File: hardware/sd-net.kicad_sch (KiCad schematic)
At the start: 13 parts, among them U1 GL823K-HCY04

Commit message: stop downward net labels colliding with their own symbols
Global labels below a pin were justified so they rendered back up over the part
they belong to: R1's LED_A sat on the resistor body and PWR_FLAG's GND was
inside the flag graphic. Flipped the justification on downward labels, then
moved R1, LED1 and the flag into their own row -- R1 had been directly below
C1, so once the labels pointed the right way C1's GND ran into R1's VDD.

Verified by rendering the PDF and inspecting it rather than by eye. ERC clean,
netlist unchanged and still passing.
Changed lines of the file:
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@@
 		(instances
 			(project "sd-net"
-				(path "/1ebe58e1-8cab-4a64-8f47-26625183a810"
+				(path "/c22e1f68-a25e-4be5-9891-1892730bf935"
 					(reference "U1") (unit 1)
 				)
@@
 		(instances
 			(project "sd-net"
-				(path "/1ebe58e1-8cab-4a64-8f47-26625183a810"
+				(path "/c22e1f68-a25e-4be5-9891-1892730bf935"
 					(reference "CARD1") (unit 1)
 				)
@@
 		(instances
 			(project "sd-net"
-				(path "/1ebe58e1-8cab-4a64-8f47-26625183a810"
+				(path "/c22e1f68-a25e-4be5-9891-1892730bf935"
 					(reference "USB1") (unit 1)
 				)
@@
 		(instances
 			(project "sd-net"
-				(path "/1ebe58e1-8cab-4a64-8f47-26625183a810"
+				(path "/c22e1f68-a25e-4be5-9891-1892730bf935"
 					(reference "C1") (unit 1)
 				)
@@
 		(instances
 			(project "sd-net"
-				(path "/1ebe58e1-8cab-4a64-8f47-26625183a810"
+				(path "/c22e1f68-a25e-4be5-9891-1892730bf935"
 					(reference "C4") (unit 1)
 				)
@@
 		(instances
 			(project "sd-net"
-				(path "/1ebe58e1-8cab-4a64-8f47-26625183a810"
+				(path "/c22e1f68-a25e-4be5-9891-1892730bf935"
 					(reference "C2") (unit 1)
 				)
@@
 		(instances
 			(project "sd-net"
-				(path "/1ebe58e1-8cab-4a64-8f47-26625183a810"
+				(path "/c22e1f68-a25e-4be5-9891-1892730bf935"
 					(reference "C5") (unit 1)
 				)
@@
 		(instances
 			(project "sd-net"
-				(path "/1ebe58e1-8cab-4a64-8f47-26625183a810"
+				(path "/c22e1f68-a25e-4be5-9891-1892730bf935"
 					(reference "C6") (unit 1)
 				)
@@
 		(instances
 			(project "sd-net"
-				(path "/1ebe58e1-8cab-4a64-8f47-26625183a810"
+				(path "/c22e1f68-a25e-4be5-9891-1892730bf935"
 					(reference "C8") (unit 1)
 				)
@@
 		(instances
 			(project "sd-net"
-				(path "/1ebe58e1-8cab-4a64-8f47-26625183a810"
+				(path "/c22e1f68-a25e-4be5-9891-1892730bf935"
 					(reference "C3") (unit 1)
 				)
@@
 		(instances
 			(project "sd-net"
-				(path "/1ebe58e1-8cab-4a64-8f47-26625183a810"
+				(path "/c22e1f68-a25e-4be5-9891-1892730bf935"
 					(reference "C7") (unit 1)
 				)
@@
 	(symbol
 		(lib_id "Device:R")
-		(at 68.58 173.99 0)
+		(at 68.58 184.15 0)
 		(unit 1)
 		(exclude_from_sim no)
@@
 		(fields_autoplaced yes)
 		(property "Reference" "R1"
-			(at 72.39 172.72 0)
+			(at 72.39 182.88 0)
 			(effects (font (size 1.27 1.27)) (justify left))
 		)
 		(property "Value" "220"
-			(at 72.39 175.26 0)
+			(at 72.39 185.42 0)
 			(effects (font (size 1.27 1.27)) (justify left))
 		)
 		(property "Footprint" "Resistor_SMD:R_0603_1608Metric"
-			(at 68.58 173.99 0)
+			(at 68.58 184.15 0)
 			(effects (font (size 1.27 1.27)) (hide yes))
 		)
 		(property "LCSC" "C22962"
-			(at 68.58 173.99 0)
-			(effects (font (size 1.27 1.27)) (hide yes))
-		)
-		(instances
-			(project "sd-net"
-				(path "/1ebe58e1-8cab-4a64-8f47-26625183a810"
+			(at 68.58 184.15 0)
+			(effects (font (size 1.27 1.27)) (hide yes))
+		)
+		(instances
+			(project "sd-net"
+				(path "/c22e1f68-a25e-4be5-9891-1892730bf935"
 					(reference "R1") (unit 1)
 				)
@@
 	(symbol
 		(lib_id "Device:LED")
-		(at 96.52 173.99 0)
+		(at 109.22 184.15 0)
 		(unit 1)
 		(exclude_from_sim no)
@@
 		(fields_autoplaced yes)
 		(property "Reference" "LED1"
-			(at 96.52 168.91 0)
+			(at 109.22 179.07 0)
 			(effects (font (size 1.27 1.27)))
 		)
 		(property "Value" "12-215SYGC"
-			(at 96.52 171.45 0)
+			(at 109.22 181.60999999999999 0)
 			(effects (font (size 1.27 1.27)))
 		)
 		(property "Footprint" "LED_SMD:LED_0603_1608Metric"
-			(at 96.52 173.99 0)
+			(at 109.22 184.15 0)
 			(effects (font (size 1.27 1.27)) (hide yes))
 		)
 		(property "LCSC" "C131283"
-			(at 96.52 173.99 0)
-			(effects (font (size 1.27 1.27)) (hide yes))
-		)
-		(instances
-			(project "sd-net"
-				(path "/1ebe58e1-8cab-4a64-8f47-26625183a810"
+			(at 109.22 184.15 0)
+			(effects (font (size 1.27 1.27)) (hide yes))
+		)
+		(instances
+			(project "sd-net"
+				(path "/c22e1f68-a25e-4be5-9891-1892730bf935"
 					(reference "LED1") (unit 1)
 				)
@@
 	(symbol
 		(lib_id "power:PWR_FLAG")
-		(at 60.96 190.5 0)
+		(at 170.18 184.15 0)
 		(unit 1)
 		(exclude_from_sim no)
@@
 		(fields_autoplaced yes)
 		(property "Reference" "#FLG01"
-			(at 64.77 189.23 0)
+			(at 173.99 182.88 0)
 			(effects (font (size 1.27 1.27)) (justify left))
 		)
 		(property "Value" "PWR_FLAG"
-			(at 64.77 191.76999999999998 0)
+			(at 173.99 185.42 0)
 			(effects (font (size 1.27 1.27)) (justify left))
 		)
 		(property "Footprint" ""
-			(at 60.96 190.5 0)
+			(at 170.18 184.15 0)
 			(effects (font (size 1.27 1.27)) (hide yes))
 		)
 		(property "LCSC" ""
-			(at 60.96 190.5 0)
-			(effects (font (size 1.27 1.27)) (hide yes))
-		)
-		(instances
-			(project "sd-net"
-				(path "/1ebe58e1-8cab-4a64-8f47-26625183a810"
+			(at 170.18 184.15 0)
+			(effects (font (size 1.27 1.27)) (hide yes))
+		)
+		(instances
+			(project "sd-net"
+				(path "/c22e1f68-a25e-4be5-9891-1892730bf935"
 					(reference "#FLG01") (unit 1)
 				)
@@
 	)
 	(wire
-		(pts (xy 68.58 170.18) (xy 68.58 166.37))
+		(pts (xy 68.58 180.34) (xy 68.58 176.53))
 		(stroke (width 0) (type default))
 	)
 	(global_label "VDD"
 		(shape bidirectional)
-		(at 68.58 166.37 90)
+		(at 68.58 176.53 90)
 		(fields_autoplaced yes)
 		(effects (font (size 1.27 1.27)) (justify left))
@@
 		(at 68.58 156.21 270)
 		(fields_autoplaced yes)
-		(effects (font (size 1.27 1.27)) (justify left))
+		(effects (font (size 1.27 1.27)) (justify right))
 	)
 	(wire
@@
 		(at 109.22 156.21 270)
 		(fields_autoplaced yes)
-		(effects (font (size 1.27 1.27)) (justify left))
+		(effects (font (size 1.27 1.27)) (justify right))
 	)
 	(wire
@@
 		(at 190.5 156.21 270)
 		(fields_autoplaced yes)
-		(effects (font (size 1.27 1.27)) (justify left))
+		(effects (font (size 1.27 1.27)) (justify right))
 	)
 	(wire
@@
 		(at 88.9 156.21 270)
 		(fields_autoplaced yes)
-		(effects (font (size 1.27 1.27)) (justify left))
+		(effects (font (size 1.27 1.27)) (justify right))
 	)
 	(wire
@@
 		(at 129.54 156.21 270)
 		(fields_autoplaced yes)
-		(effects (font (size 1.27 1.27)) (justify left))
+		(effects (font (size 1.27 1.27)) (justify right))
 	)
 	(wire
@@
 		(at 149.86 156.21 270)
 		(fields_autoplaced yes)
-		(effects (font (size 1.27 1.27)) (justify left))
+		(effects (font (size 1.27 1.27)) (justify right))
 	)
 	(wire
@@
 		(at 210.82 156.21 270)
 		(fields_autoplaced yes)
-		(effects (font (size 1.27 1.27)) (justify left))
+		(effects (font (size 1.27 1.27)) (justify right))
 	)
 	(wire
@@
 		(at 170.18 156.21 270)
 		(fields_autoplaced yes)
-		(effects (font (size 1.27 1.27)) (justify left))
+		(effects (font (size 1.27 1.27)) (justify right))
 	)
 	(wire
@@
 	)
 	(wire
-		(pts (xy 68.58 177.8) (xy 68.58 181.61))
+		(pts (xy 68.58 187.96) (xy 68.58 191.77))
 		(stroke (width 0) (type default))
 	)
 	(global_label "LED_A"
 		(shape bidirectional)
-		(at 68.58 181.61 270)
-		(fields_autoplaced yes)
-		(effects (font (size 1.27 1.27)) (justify left))
-	)
-	(wire
-		(pts (xy 100.33 173.99) (xy 104.14 173.99))
+		(at 68.58 191.77 270)
+		(fields_autoplaced yes)
+		(effects (font (size 1.27 1.27)) (justify right))
+	)
+	(wire
+		(pts (xy 113.03 184.15) (xy 116.84 184.15))
 		(stroke (width 0) (type default))
 	)
 	(global_label "LED_A"
 		(shape bidirectional)
-		(at 104.14 173.99 0)
-		(fields_autoplaced yes)
-		(effects (font (size 1.27 1.27)) (justify left))
-	)
-	(wire
-		(pts (xy 92.71 173.99) (xy 88.89999999999999 173.99))
+		(at 116.84 184.15 0)
+		(fields_autoplaced yes)
+		(effects (font (size 1.27 1.27)) (justify left))
+	)
+	(wire
+		(pts (xy 105.41 184.15) (xy 101.6 184.15))
 		(stroke (width 0) (type default))
 	)
 	(global_label "LED_K"
 		(shape bidirectional)
-		(at 88.89999999999999 173.99 180)
+		(at 101.6 184.15 180)
 		(fields_autoplaced yes)
 		(effects (font (size 1.27 1.27)) (justify right))
@@
 	)
 	(wire
-		(pts (xy 60.96 190.5) (xy 60.96 194.31))
-		(stroke (width 0) (type default))
-	)
-	(global_label "GND"
-		(shape bidirectional)
-		(at 60.96 194.31 270)
-		(fields_autoplaced yes)
-		(effects (font (size 1.27 1.27)) (justify left))
+		(pts (xy 170.18 184.15) (xy 170.18 187.96))
+		(stroke (width 0) (type default))
+	)
+	(global_label "GND"
+		(shape bidirectional)
+		(at 170.18 187.96 270)
+		(fields_autoplaced yes)
+		(effects (font (size 1.27 1.27)) (justify right))
 	)
 	(sheet_instances

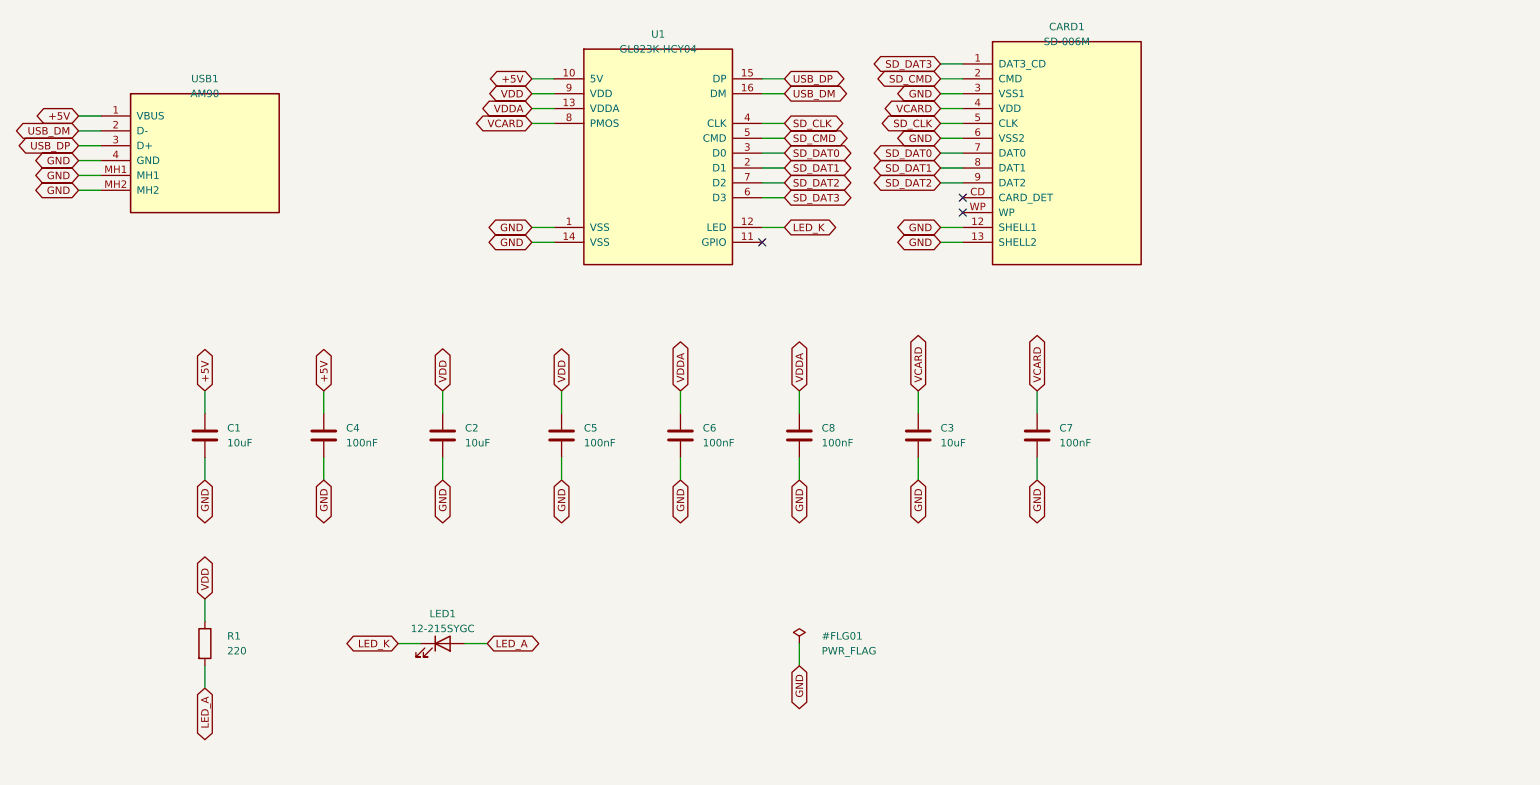
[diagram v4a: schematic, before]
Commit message: put component values on the board instead of footprint names
A .kicad_mod's Value property holds the footprint name, and gen_pcb.py embedded
it unchanged -- so every part on the board read C_0805_2012Metric or
SSOP-16_3.9x4.9mm_P0.635mm rather than 10uF or GL823K-HCY04. The value was
already being passed into place(); it just was not used. Beyond cluttering the
canvas this would have produced a meaningless fab BOM.
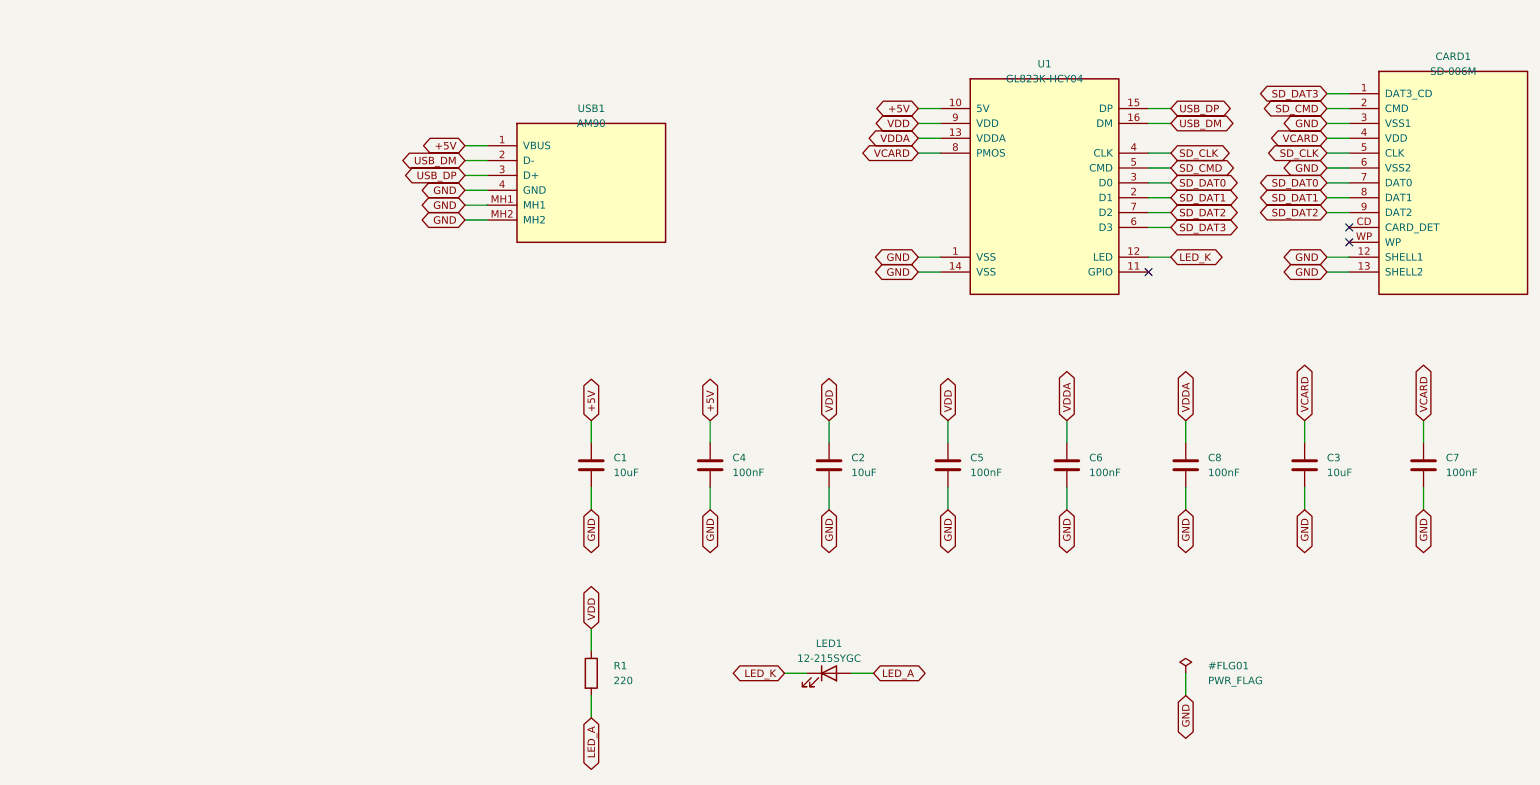
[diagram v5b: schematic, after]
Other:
- company: (none) -> PhoneTucked
- title: (none) -> sd - net 2.0 
- moved on the sheet: C1, C2, C3, C4, C5, C6, C7, C8, CARD1, LED1, R1, U1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

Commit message: add manufacturer part numbers for the PCBWay BOM
PCBWay sources on the open market and quotes from manufacturer part numbers;
the schematic only carried LCSC codes, which are JLCPCB's system. Every symbol
now also has MPN and Manufacturer, so the exported BOM is quotable as-is.

Recovered from the rev 1.5 BOM: GL823K-HCY04 (Genesys), CL21A106KAYNNNE
(Samsung), CC0603KRX7R9BB104 (Yageo), 0603WAF2200T5E (Uni-Royal),
12-215SYGC/S530-E2/TR8 (Everlight), SD-006M (Sofng), AM90 (Shou Han).

Mechanical diff against rev 1.5 passes: board width identical to three decimal
places at 113.854 mm, main outline height identical at 60.291 mm, and all five
drill sizes match within a hundredth. The only outline difference is the
12.40 x 15.40 mm connector-body rectangle we deliberately excluded.

Fab package written to the Desktop, not the repo -- hardware/build is
gitignored and these are regenerable.
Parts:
- C1, C2, C3: MPN (none) -> CL21A106KAYNNNE; Manufacturer (none) -> Samsung
- C4, C5, C6, C7, C8: MPN (none) -> CC0603KRX7R9BB104; Manufacturer (none) -> Yageo
- CARD1: MPN (none) -> SD-006M; Manufacturer (none) -> Sofng
- LED1: MPN (none) -> 12-215SYGC/S530-E2/TR8; Manufacturer (none) -> Everlight
- R1: MPN (none) -> 0603WAF2200T5E; Manufacturer (none) -> Uni-Royal
- U1: MPN (none) -> GL823K-HCY04; Manufacturer (none) -> Genesys Logic
- USB1: MPN (none) -> AM90; Manufacturer (none) -> Shou Han

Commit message: correct four footprints against the manufacturers' land patterns
gen_footprints.py built SD-006M, USB-AM90 and the LED land from rev 1.5's
fabricated pads, on the reasoning that pads boards were built with must match
the physical parts. Rev 1.5 never enumerated, so that reasoning was never
actually tested. Measured against the manufacturers' own recommended layouts,
four things were wrong.

SD-006M: the contact row sat 24.05 mm from the mounting pegs; the datasheet
says 24.60. The pegs locate the socket, so the tails were landing ~0.55 mm off
the pads -- about 78% overlap on a 2.0 mm tail. Marginal rather than fatal,
which is exactly why nothing caught it. Confirmed three ways: the printed 24.6
dimension, the drawn geometry, and rev 1.5's own CPL and drill file. CD and WP
also had the wrong X, and they are the only two contacts this design leaves
unconnected -- which says something about how that library was drawn.

USB-AM90: the locating pegs were 0.175 mm out against 0.05-0.075 mm of
clearance, so the plug would bind rather than seat flat. And the AM90 has no
mounting posts -- its shell ends in two flat 0.86 mm tabs that belong in slots,
not the 2.6 mm round holes rev 1.5 drilled. Those tabs are the only thing
anchoring a board that cantilevers 75 mm out of a USB port, so BEFORE-ORDERING
open item 5 is corrected too.

LED1: a rev 2.0 regression rather than a rev 1.5 one. The schematic kept the
Everlight MPN but the PCB assigned it a stock 0603 land, under a part that is
2.0 x 1.0 mm. Now on a part-specific land, with a silkscreen cathode bar --
the generated footprints carry no polarity marking of their own.

Behind the SD move: seven SD-bus tracks followed their pads with no change of
topology, the VCARD via moved 0.25 mm clear of pad 3, and C7 moved 0.5 mm.
That last one also restores the gap between C7's VCARD pad and CARD1's GND
contact, which the row move had cut from 0.912 mm to 0.363 mm. A bridge there
would tie VCARD to ground, which is the rev 1.5 failure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
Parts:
- LED1: footprint LED_SMD:LED_0603_1608Metric -> sd-net:LED-12-215SYGC
